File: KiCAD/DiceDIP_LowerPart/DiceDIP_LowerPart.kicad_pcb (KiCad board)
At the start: 2 copper layers, 40 x 40 mm, 21 parts, among them J1 Conn_01x03, J4 Conn_01x06, Q1 BC547, U1 4029, U2 4093

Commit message: routing upper side done
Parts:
- moved R1 12.9 mm to (126.6, 91.3)
- moved C1 12.5 mm to (134.1, 78.9), turned to 180 degrees
- moved D11 10.1 mm to (117.0, 112.0), turned to 180 degrees
- moved D9 9.18 mm to (113.7, 108.8), turned to 180 degrees
- moved C4 8.62 mm to (102.3, 103.0)
- moved R4 8.55 mm to (126.6, 82.0)
- moved D10 7.61 mm to (113.7, 106.0), turned to 180 degrees
- moved D1 7.60 mm to (113.8, 99.8)
- moved R2 5.75 mm to (126.6, 88.2)
- moved C2 3.26 mm to (105.4, 103.0)
- moved R5 1.45 mm to (120.7, 105.4), turned to -90 degrees
- moved R3 1.40 mm to (126.6, 85.1)
- moved Q1 1.23 mm to (135.3, 99.0)
- moved C3 0.60 mm to (102.9, 78.6), turned to -45 degrees
- moved J4 0.46 mm to (137.5, 78.5)
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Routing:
- net Net-(D9-A): track 0.00 -> 97.4 mm, vias 0 -> 1
- net Net-(C3-Pad2): track 0.00 -> 69.4 mm, vias 0 -> 4
- net Net-(J4-Pin_1): track 0.00 -> 63.5 mm
- net Net-(D1-K): track 0.00 -> 63.3 mm
- net SW_V2: track 0.00 -> 61.2 mm, vias 0 -> 2
- net VCC: track 0.00 -> 50.8 mm, vias 0 -> 2
- net Net-(U1-PE): track 0.00 -> 47.6 mm, vias 0 -> 5
- net Net-(BT1-+): track 0.00 -> 42.9 mm
- net Net-(U1-Cout): track 0.00 -> 40.1 mm
- net Net-(R5-Pad1): track 0.00 -> 37.0 mm
- net Net-(Q1-B): track 0.00 -> 32.7 mm
- net Net-(BT1--): track 0.00 -> 31.1 mm
- net Net-(J4-Pin_2): track 0.00 -> 28.9 mm, vias 0 -> 3
- net Net-(D10-A): track 0.00 -> 26.7 mm, vias 0 -> 3
- net Net-(C1-Pad2): track 0.00 -> 25.1 mm, vias 0 -> 2
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
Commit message: minor changes
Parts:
- moved C2 33.1 mm to (137.5, 95.0), turned to -90 degrees
- moved C4 33.0 mm to (134.2, 94.8), turned to -90 degrees
- moved C3 31.3 mm to (124.8, 101.0), turned to -90 degrees
- moved J1 27.5 mm to (130.0, 106.0)
- moved J4 27.5 mm to (110.0, 78.0), turned to 90 degrees
- moved R2 25.2 mm to (101.8, 92.3), turned to 90 degrees
- moved D10 23.8 mm to (136.8, 111.8), turned to 90 degrees
- moved R10 23.7 mm to (101.8, 107.1)
- moved U2 22.5 mm to (105.0, 107.0), turned to 90 degrees
- moved R1 21.6 mm to (105.0, 92.3), turned to 90 degrees
- moved D9 20.5 mm to (134.0, 111.8), turned to 90 degrees
- moved Q1 19.8 mm to (134.2, 79.3)
- moved C1 18.2 mm to (117.0, 85.0)
- moved R4 17.4 mm to (109.2, 81.8)
- moved U1 16.6 mm to (119.8, 91.4), turned to 90 degrees
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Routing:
- net Net-(D9-A): track 97.4 -> 55.3 mm, vias 1 -> 2
- net VCC: track 50.8 -> 90.8 mm, vias 2 -> 3
- net Net-(U1-PE): track 47.6 -> 9.99 mm, vias 5 -> 1
- net SW_V2: track 61.2 -> 97.1 mm
- net SW_V1: track 0.00 -> 33.6 mm
- net Net-(J4-Pin_1): track 63.5 -> 31.2 mm, vias 0 -> 2
- net Net-(BT1--): track 31.1 -> 3.45 mm
- net Net-(Q1-B): track 32.7 -> 56.9 mm
- net Net-(BT1-+): track 42.9 -> 20.7 mm
- net Net-(R5-Pad1): track 37.0 -> 15.0 mm
- net Net-(C3-Pad2): track 69.4 -> 48.2 mm, vias 4 -> 8
- net Net-(U1-Cout): track 40.1 -> 19.8 mm, vias 0 -> 4
- net Net-(D10-K): track 20.3 -> 7.05 mm
- net Net-(D1-A): track 12.9 -> 23.0 mm, vias 0 -> 1
- net Net-(D10-A): track 26.7 -> 33.7 mm, vias 3 -> 0
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- removed copper zone on F.Cu, net VCC

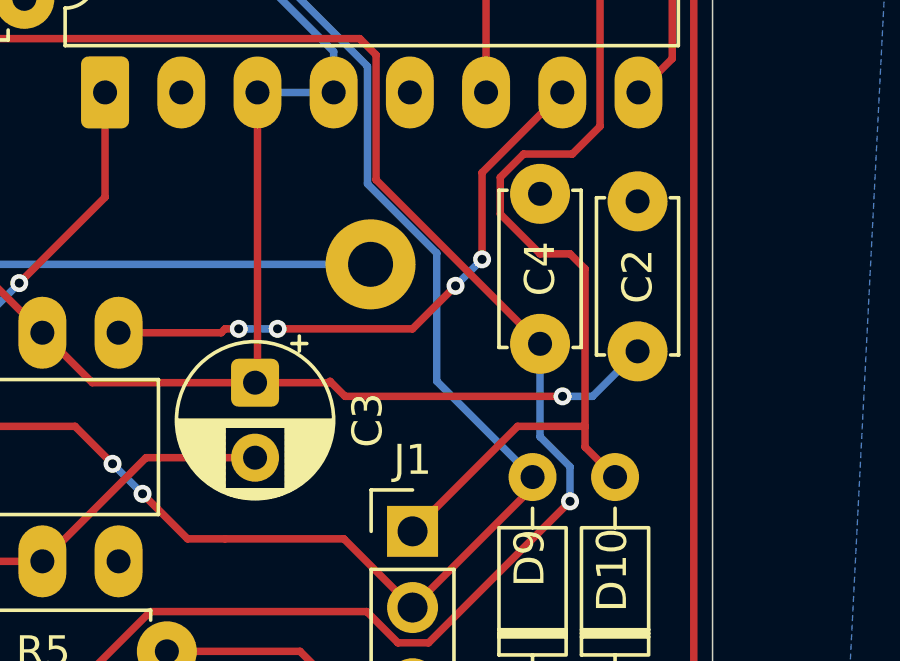
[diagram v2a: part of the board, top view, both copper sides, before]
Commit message: added submodule and added legal stuff on lowerPart
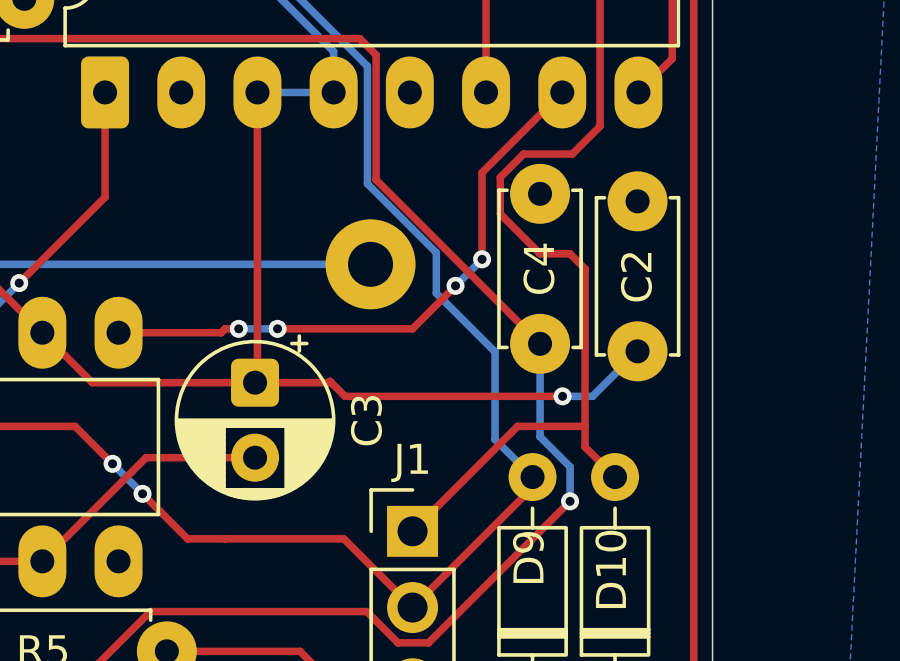
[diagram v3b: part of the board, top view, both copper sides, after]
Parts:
- added blinkyparts_logo_5mm: G***, blinkyparts:logo_blinkyparts_5mm_F.Mask, B.Cu at (106.5, 76.8)
- added ce-symbol_mask_3mm: G***, blinkyparts:legislation_ce-icon_3mm_F.Mask, B.Cu at (131.8, 100.0)
- added weee-symbol_mask_3mm: G***, blinkyparts:legislation_weee-icon_3mm_F.Mask, B.Cu at (133.9, 86.6)
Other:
- board text added: "Product & Design by blinkyparts.com Egerstr. 9, 93057 R"

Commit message: added name and version. Created gerber files for lowerPart
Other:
- board text added: "DiceDIP LowerPart v2.0"
- board text added: "Product & Design by blinkyparts.com Egerstr. 9, 93057 Regensburg"
- board text removed: "Product & Design by blinkyparts.com Egerstr. 9, 93057 R"

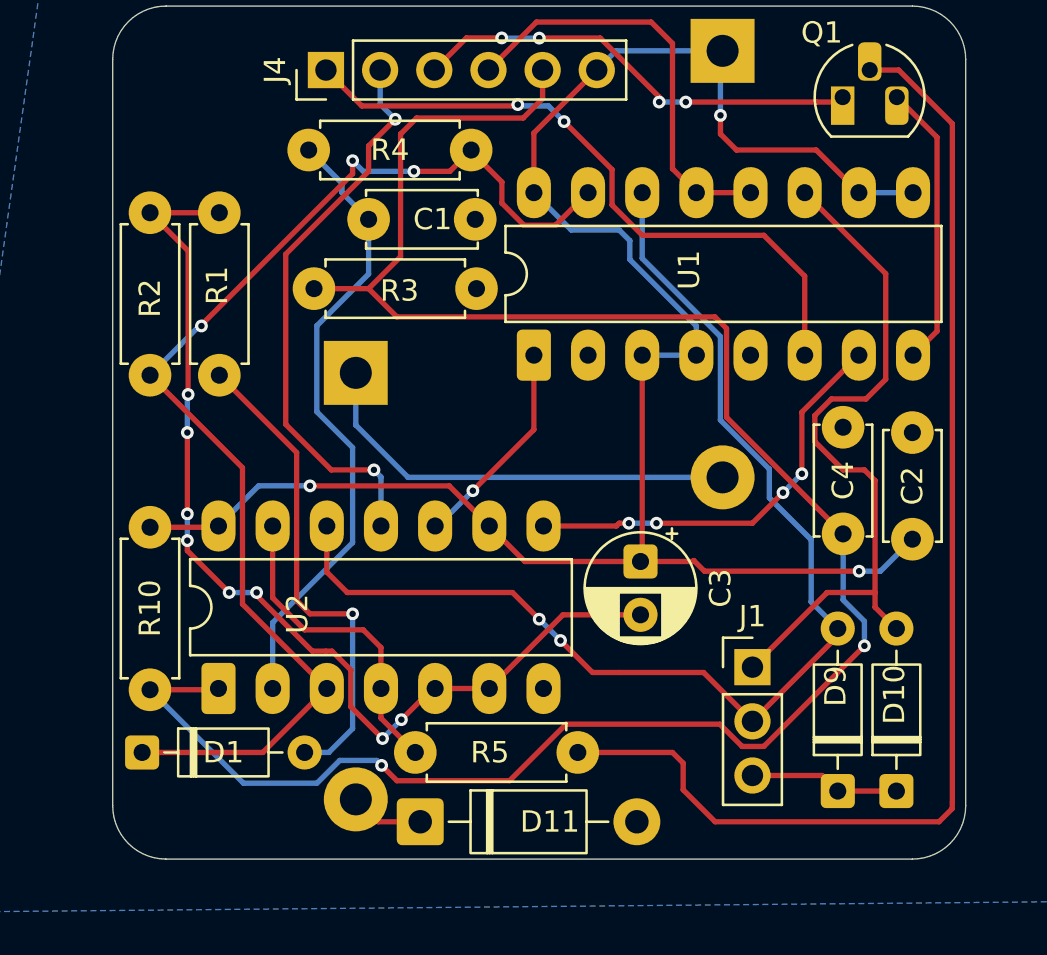
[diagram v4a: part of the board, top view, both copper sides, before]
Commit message: changed some silkscreen and updated gerber-files
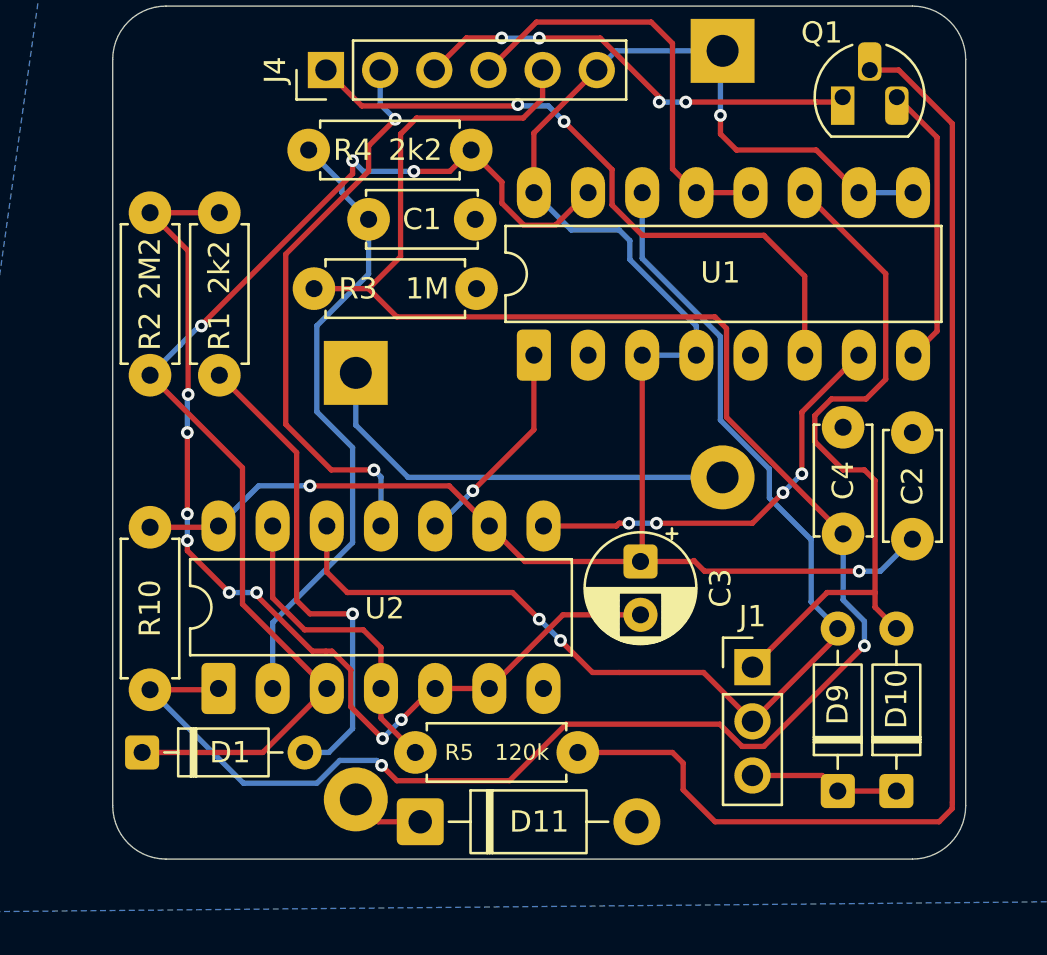
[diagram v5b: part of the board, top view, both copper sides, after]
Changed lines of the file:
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@@
 		(tags "Resistor Axial_DIN0207 series Axial Horizontal pin pitch 7.62mm 0.25W = 1/4W length 6.3mm diameter 2.5mm")
 		(property "Reference" "R4"
-			(at 3.81 0 0)
+			(at 2.06 0 0)
 			(layer "F.SilkS")
 			(effects
@@
 		(property "Value" "2k2"
 			(at 5 0 0)
-			(layer "F.Fab")
+			(layer "F.SilkS")
 			(effects
 				(font
@@
 		(tags "C Disc series Radial pin pitch 5.00mm diameter 5mm width 2.5mm Capacitor")
 		(property "Reference" "C1"
-			(at 2 0 0)
+			(at 2.5 0 0)
 			(layer "F.SilkS")
 			(effects
@@
 		(tags "THT DIP DIL PDIP 2.54mm 7.62mm 300mil LongPads")
 		(property "Reference" "U1"
-			(at 4 7.28 90)
+			(at 3.87 8.75 180)
 			(layer "F.SilkS")
 			(effects
@@
 		(tags "Diode DO-41_SOD81 series Axial Horizontal pin pitch 10.16mm  length 5.2mm diameter 2.7mm")
 		(property "Reference" "D11"
-			(at 6.08 0 0)
+			(at 5.58 0 0)
 			(layer "F.SilkS")
 			(effects
@@
 		(tags "Resistor Axial_DIN0207 series Axial Horizontal pin pitch 7.62mm 0.25W = 1/4W length 6.3mm diameter 2.5mm")
 		(property "Reference" "R2"
-			(at 3.61 0 90)
+			(at 2.06 0 90)
 			(layer "F.SilkS")
 			(effects
@@
 		(property "Value" "2M2"
 			(at 5 0 90)
-			(layer "F.Fab")
+			(layer "F.SilkS")
 			(effects
 				(font
@@
 		(tags "Resistor Axial_DIN0207 series Axial Horizontal pin pitch 7.62mm 0.25W = 1/4W length 6.3mm diameter 2.5mm")
 		(property "Reference" "R3"
-			(at 3.61 -0.1 0)
+			(at 5.56 0 0)
 			(layer "F.SilkS")
 			(effects
@@
 		)
 		(property "Value" "1M"
-			(at 5 0 0)
-			(layer "F.Fab")
+			(at 2.31 0 0)
+			(layer "F.SilkS")
 			(effects
 				(font
@@
 		(tags "Resistor Axial_DIN0207 series Axial Horizontal pin pitch 7.62mm 0.25W = 1/4W length 6.3mm diameter 2.5mm")
 		(property "Reference" "R1"
-			(at 4.21 -0.1 90)
+			(at 2.06 0 90)
 			(layer "F.SilkS")
 			(effects
@@
 		)
 		(property "Value" "2k2"
-			(at 5 0 90)
-			(layer "F.Fab")
+			(at 5.06 0 90)
+			(layer "F.SilkS")
 			(effects
 				(font
@@
 		(tags "Diode DO-35_SOD27 series Axial Horizontal pin pitch 7.62mm  length 4mm diameter 2mm")
 		(property "Reference" "D1"
-			(at 3.81 0 0)
+			(at 4.12 0 0)
 			(layer "F.SilkS")
 			(effects
@@
 		(tags "Diode DO-35_SOD27 series Axial Horizontal pin pitch 7.62mm  length 4mm diameter 2mm")
 		(property "Reference" "D9"
-			(at 4.92 -0.1 90)
+			(at 4.06 0 90)
 			(layer "F.SilkS")
 			(effects
@@
 		(tags "Diode DO-35_SOD27 series Axial Horizontal pin pitch 7.62mm  length 4mm diameter 2mm")
 		(property "Reference" "D10"
-			(at 4.52 -0.1 90)
+			(at 4.31 0 90)
 			(layer "F.SilkS")
 			(effects
@@
 		(tags "Resistor Axial_DIN0207 series Axial Horizontal pin pitch 7.62mm 0.25W = 1/4W length 6.3mm diameter 2.5mm")
 		(property "Reference" "R5"
-			(at 3.5 0 0)
+			(at 2.06 0 0)
 			(layer "F.SilkS")
 			(effects
 				(font
-					(size 1 1)
-					(thickness 0.15)
+					(size 0.75 0.75)
+					(thickness 0.1)
 				)
 			)
@@
 		(property "Value" "120k"
 			(at 5 0 0)
-			(layer "F.Fab")
+			(layer "F.SilkS")
 			(effects
 				(font
-					(size 1 1)
-					(thickness 0.15)
+					(size 0.75 0.75)
+					(thickness 0.1)
 				)
 			)
@@
 		(tags "THT DIP DIL PDIP 2.54mm 7.62mm 300mil LongPads")
 		(property "Reference" "U2"
-			(at 3.5 3.7 90)
+			(at 3.75 7.79 180)
 			(layer "F.SilkS")
 			(effects
